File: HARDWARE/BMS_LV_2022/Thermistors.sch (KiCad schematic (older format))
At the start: 18 parts

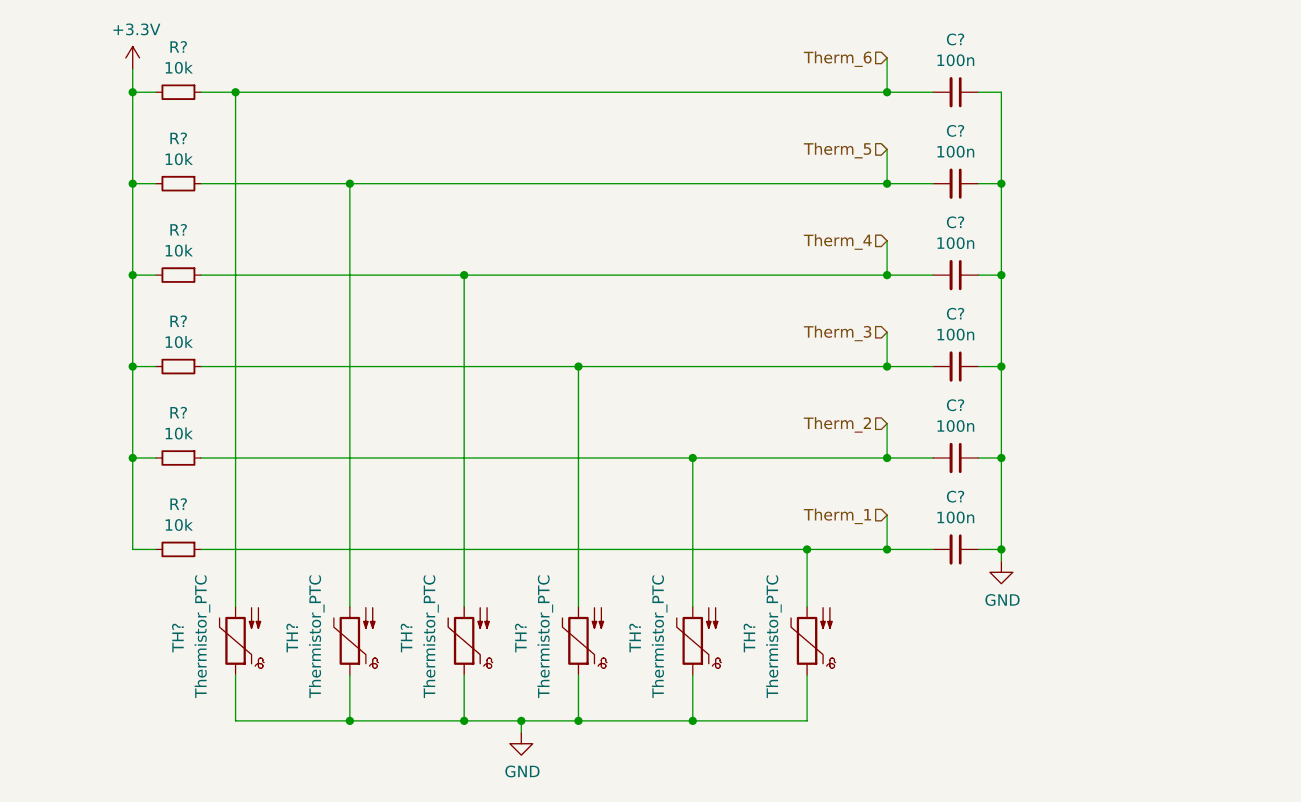
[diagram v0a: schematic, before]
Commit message: Hardware Update 2
First verison of the scheme finished
+Power section
+eFuse section
+Current Sensor section
+Connectors section
+Debug LEDs
+STM32L4P5RET6 all signals configuration
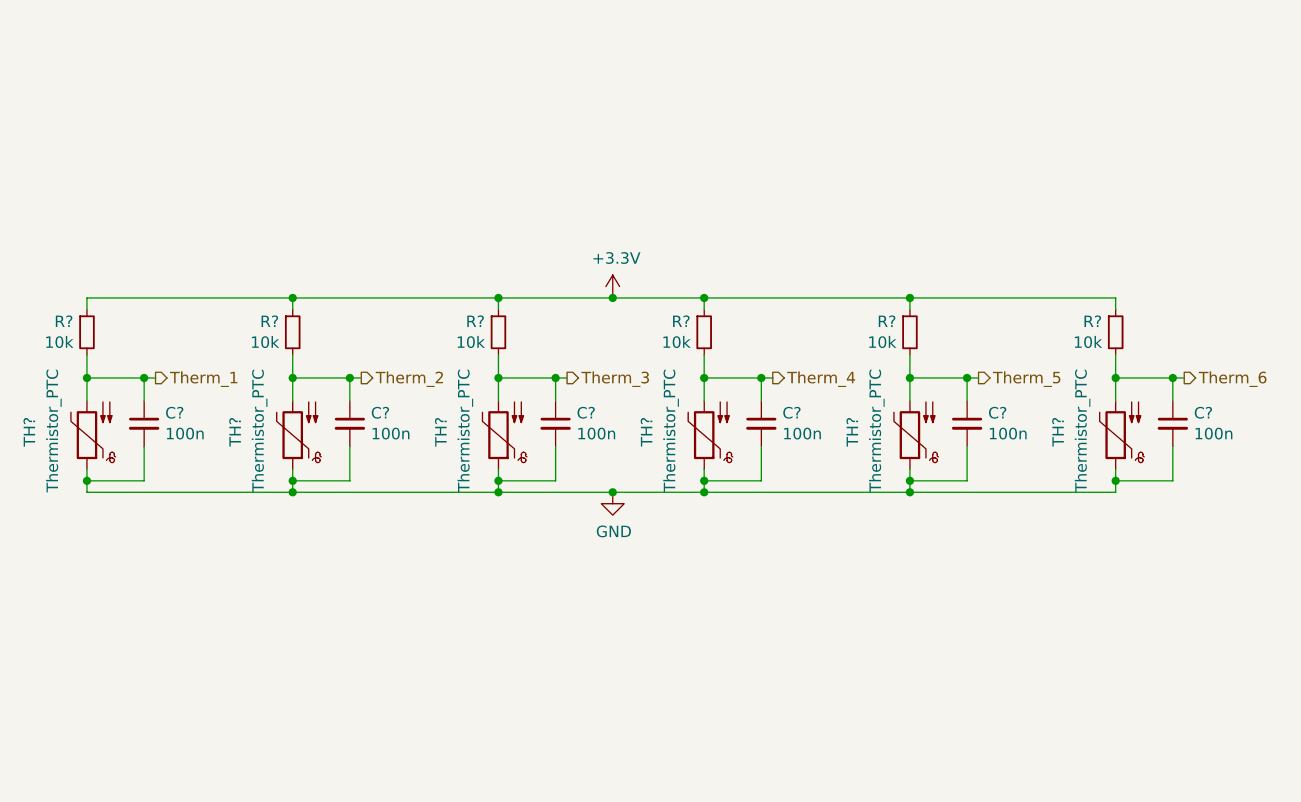
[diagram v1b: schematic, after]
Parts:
- removed C? (x6): 100n, symbol Device:C_Small
- removed R? (x6): 10k, symbol Device:R_Small
- removed TH? (x5): Thermistor_PTC, symbol Device:Thermistor_PTC
- added C? (x6): 100n, symbol Device:C_Small
- added R? (x6): 10k, symbol Device:R_Small
- added TH? (x5): Thermistor_PTC, symbol Device:Thermistor_PTC
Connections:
- net +3V3: now also R?.1, R?.1, R?.1, R?.1, R?.1, R?.1
- net GND: now also C?.2, C?.2, C?.2, C?.2, C?.2, C?.2, TH?.1, TH?.1, TH?.1, TH?.1, TH?.1
- net Therm_1: now also TH?.2, C?.1, R?.2
- net Therm_2: now also C?.1, R?.2, TH?.2
- net Therm_3: now also C?.1, R?.2, TH?.2
- net Therm_4: now also C?.1, R?.2, TH?.2
- net Therm_5: now also C?.1, R?.2, TH?.2
- net Therm_6: now also C?.1, R?.2, TH?.2; no longer TH?.2
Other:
- moved on the sheet: TH?

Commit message: Hardware update; -changes after team review;
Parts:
- C? (x6): value 100n -> 100nF
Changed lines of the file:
@@
 P 1300 2550
 F 0 "C?" H 1392 2596 50  0000 L CNN
-F 1 "100n" H 1392 2505 50  0000 L CNN
+F 1 "100nF" H 1392 2505 50  0000 L CNN
 F 2 "" H 1300 2550 50  0001 C CNN
 F 3 "~" H 1300 2550 50  0001 C CNN
@@
 P 2200 2550
 F 0 "C?" H 2292 2596 50  0000 L CNN
-F 1 "100n" H 2292 2505 50  0000 L CNN
+F 1 "100nF" H 2292 2505 50  0000 L CNN
 F 2 "" H 2200 2550 50  0001 C CNN
 F 3 "~" H 2200 2550 50  0001 C CNN
@@
 P 3100 2550
 F 0 "C?" H 3192 2596 50  0000 L CNN
-F 1 "100n" H 3192 2505 50  0000 L CNN
+F 1 "100nF" H 3192 2505 50  0000 L CNN
 F 2 "" H 3100 2550 50  0001 C CNN
 F 3 "~" H 3100 2550 50  0001 C CNN
@@
 P 4000 2550
 F 0 "C?" H 4092 2596 50  0000 L CNN
-F 1 "100n" H 4092 2505 50  0000 L CNN
+F 1 "100nF" H 4092 2505 50  0000 L CNN
 F 2 "" H 4000 2550 50  0001 C CNN
 F 3 "~" H 4000 2550 50  0001 C CNN
@@
 P 4900 2550
 F 0 "C?" H 4992 2596 50  0000 L CNN
-F 1 "100n" H 4992 2505 50  0000 L CNN
+F 1 "100nF" H 4992 2505 50  0000 L CNN
 F 2 "" H 4900 2550 50  0001 C CNN
 F 3 "~" H 4900 2550 50  0001 C CNN
@@
 P 5800 2550
 F 0 "C?" H 5892 2596 50  0000 L CNN
-F 1 "100n" H 5892 2505 50  0000 L CNN
+F 1 "100nF" H 5892 2505 50  0000 L CNN
 F 2 "" H 5800 2550 50  0001 C CNN
 F 3 "~" H 5800 2550 50  0001 C CNN

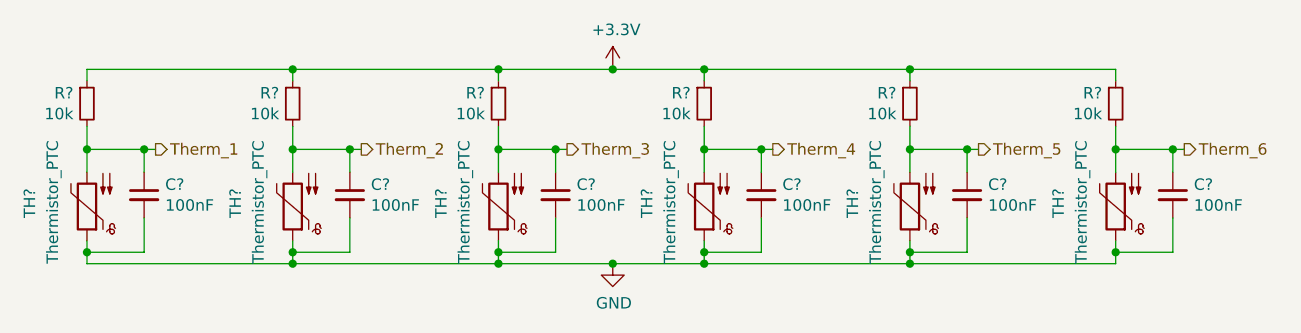
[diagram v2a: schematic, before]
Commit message: Electrical Rules Checker fixes
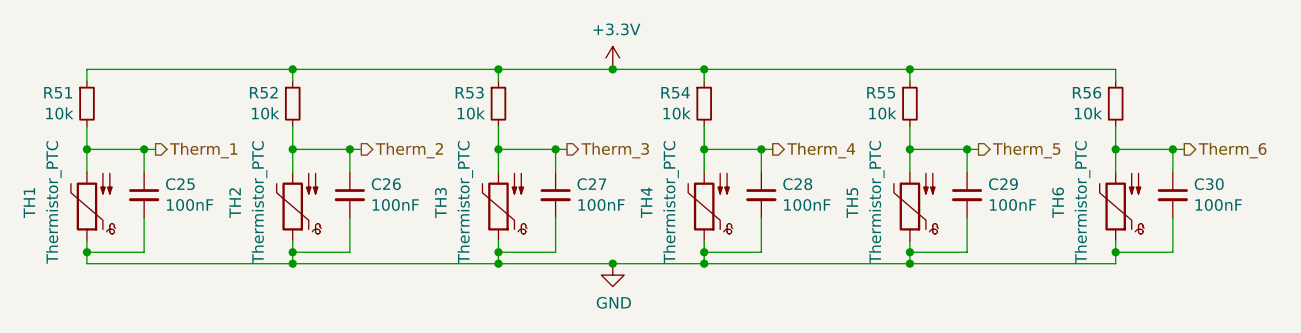
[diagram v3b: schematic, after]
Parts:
- gave numbers to parts that had none: 18
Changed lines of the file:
@@
 Therm_3
 $Comp
-L Device:Thermistor_PTC TH?
+L Device:Thermistor_PTC TH2
 U 1 1 61B219CC
 P 1950 2600
-F 0 "TH?" V 2200 2650 50  0000 R CNN
+F 0 "TH2" V 2200 2650 50  0000 R CNN
 F 1 "Thermistor_PTC" V 2100 2850 50  0000 R CNN
 F 2 "" H 2000 2400 50  0001 L CNN
@@
 	2200 2450 2200 2350
 $Comp
-L Device:Thermistor_PTC TH?
+L Device:Thermistor_PTC TH3
 U 1 1 61B244E9
 P 2850 2600
-F 0 "TH?" V 3100 2650 50  0000 R CNN
+F 0 "TH3" V 3100 2650 50  0000 R CNN
 F 1 "Thermistor_PTC" V 3000 2850 50  0000 R CNN
 F 2 "" H 2900 2400 50  0001 L CNN
@@
 $EndComp
 $Comp
-L power:GND #PWR?
+L power:GND #PWR039
 U 1 1 61B244EF
 P 3350 2850
-F 0 "#PWR?" H 3350 2600 50  0001 C CNN
+F 0 "#PWR039" H 3350 2600 50  0001 C CNN
 F 1 "GND" H 3355 2677 50  0000 C CNN
 F 2 "" H 3350 2850 50  0001 C CNN
@@
 $EndComp
 $Comp
-L power:+3.3V #PWR?
+L power:+3.3V #PWR038
 U 1 1 61B244FC
 P 3350 2000
-F 0 "#PWR?" H 3350 1850 50  0001 C CNN
+F 0 "#PWR038" H 3350 1850 50  0001 C CNN
 F 1 "+3.3V" H 3365 2173 50  0000 C CNN
 F 2 "" H 3350 2000 50  0001 C CNN
@@
 	5550 2000 5550 2050
 $Comp
-L Device:Thermistor_PTC TH?
+L Device:Thermistor_PTC TH6
 U 1 1 61B31D1D
 P 5550 2600
-F 0 "TH?" V 5800 2650 50  0000 R CNN
+F 0 "TH6" V 5800 2650 50  0000 R CNN
 F 1 "Thermistor_PTC" V 5700 2850 50  0000 R CNN
 F 2 "" H 5600 2400 50  0001 L CNN
@@
 	4650 2000 4650 2050
 $Comp
-L Device:Thermistor_PTC TH?
+L Device:Thermistor_PTC TH5
 U 1 1 61B2C7C1
 P 4650 2600
-F 0 "TH?" V 4900 2650 50  0000 R CNN
+F 0 "TH5" V 4900 2650 50  0000 R CNN
 F 1 "Thermistor_PTC" V 4800 2850 50  0000 R CNN
 F 2 "" H 4700 2400 50  0001 L CNN
@@
 	3750 2000 3750 2050
 $Comp
-L Device:Thermistor_PTC TH?
+L Device:Thermistor_PTC TH4
 U 1 1 61B27A00
 P 3750 2600
-F 0 "TH?" V 4000 2650 50  0000 R CNN
+F 0 "TH4" V 4000 2650 50  0000 R CNN
 F 1 "Thermistor_PTC" V 3900 2850 50  0000 R CNN
 F 2 "" H 3800 2400 50  0001 L CNN
@@
 Connection ~ 3350 2850
 $Comp
-L Device:R_Small R?
+L Device:R_Small R52
 U 1 1 62CFDB9E
 P 1950 2150
-F 0 "R?" H 1891 2196 50  0000 R CNN
+F 0 "R52" H 1891 2196 50  0000 R CNN
 F 1 "10k" H 1891 2105 50  0000 R CNN
 F 2 "" H 1950 2150 50  0001 C CNN
@@
 $EndComp
 $Comp
-L Device:R_Small R?
+L Device:R_Small R53
 U 1 1 62CFF2A0
 P 2850 2150
-F 0 "R?" H 2791 2196 50  0000 R CNN
+F 0 "R53" H 2791 2196 50  0000 R CNN
 F 1 "10k" H 2791 2105 50  0000 R CNN
 F 2 "" H 2850 2150 50  0001 C CNN
@@
 $EndComp
 $Comp
-L Device:R_Small R?
+L Device:R_Small R54
 U 1 1 62D007FE
 P 3750 2150
-F 0 "R?" H 3691 2196 50  0000 R CNN
+F 0 "R54" H 3691 2196 50  0000 R CNN
 F 1 "10k" H 3691 2105 50  0000 R CNN
 F 2 "" H 3750 2150 50  0001 C CNN
@@
 $EndComp
 $Comp
-L Device:R_Small R?
+L Device:R_Small R55
 U 1 1 62D01C61
 P 4650 2150
-F 0 "R?" H 4591 2196 50  0000 R CNN
+F 0 "R55" H 4591 2196 50  0000 R CNN
 F 1 "10k" H 4591 2105 50  0000 R CNN
 F 2 "" H 4650 2150 50  0001 C CNN
@@
 $EndComp
 $Comp
-L Device:R_Small R?
+L Device:R_Small R56
 U 1 1 62D030DD
 P 5550 2150
-F 0 "R?" H 5491 2196 50  0000 R CNN
+F 0 "R56" H 5491 2196 50  0000 R CNN
 F 1 "10k" H 5491 2105 50  0000 R CNN
 F 2 "" H 5550 2150 50  0001 C CNN
@@
 	1350 2350 1300 2350
 $Comp
-L Device:R_Small R?
+L Device:R_Small R51
 U 1 1 62CF3EC5
 P 1050 2150
-F 0 "R?" H 991 2196 50  0000 R CNN
+F 0 "R51" H 991 2196 50  0000 R CNN
 F 1 "10k" H 991 2105 50  0000 R CNN
 F 2 "" H 1050 2150 50  0001 C CNN
@@
 Therm_1
 $Comp
-L Device:Thermistor_PTC TH?
+L Device:Thermistor_PTC TH1
 U 1 1 61D11206
 P 1050 2600
-F 0 "TH?" V 1300 2650 50  0000 R CNN
+F 0 "TH1" V 1300 2650 50  0000 R CNN
 F 1 "Thermistor_PTC" V 1200 2850 50  0000 R CNN
 F 2 "" H 1100 2400 50  0001 L CNN
@@
 	4650 2000 5550 2000
 $Comp
-L Device:C_Small C?
+L Device:C_Small C25
 U 1 1 62D3AF1E
 P 1300 2550
-F 0 "C?" H 1392 2596 50  0000 L CNN
+F 0 "C25" H 1392 2596 50  0000 L CNN
 F 1 "100nF" H 1392 2505 50  0000 L CNN
 F 2 "" H 1300 2550 50  0001 C CNN
@@
 $EndComp
 $Comp
-L Device:C_Small C?
+L Device:C_Small C26
 U 1 1 62D3D09F
 P 2200 2550
-F 0 "C?" H 2292 2596 50  0000 L CNN
+F 0 "C26" H 2292 2596 50  0000 L CNN
 F 1 "100nF" H 2292 2505 50  0000 L CNN
 F 2 "" H 2200 2550 50  0001 C CNN
@@
 $EndComp
 $Comp
-L Device:C_Small C?
+L Device:C_Small C27
 U 1 1 62D3FB8F
 P 3100 2550
-F 0 "C?" H 3192 2596 50  0000 L CNN
+F 0 "C27" H 3192 2596 50  0000 L CNN
 F 1 "100nF" H 3192 2505 50  0000 L CNN
 F 2 "" H 3100 2550 50  0001 C CNN
@@
 $EndComp
 $Comp
-L Device:C_Small C?
+L Device:C_Small C28
 U 1 1 62D42810
 P 4000 2550
-F 0 "C?" H 4092 2596 50  0000 L CNN
+F 0 "C28" H 4092 2596 50  0000 L CNN
 F 1 "100nF" H 4092 2505 50  0000 L CNN
 F 2 "" H 4000 2550 50  0001 C CNN
@@
 $EndComp
 $Comp
-L Device:C_Small C?
+L Device:C_Small C29
 U 1 1 62D45530
 P 4900 2550
-F 0 "C?" H 4992 2596 50  0000 L CNN
+F 0 "C29" H 4992 2596 50  0000 L CNN
 F 1 "100nF" H 4992 2505 50  0000 L CNN
 F 2 "" H 4900 2550 50  0001 C CNN
@@
 $EndComp
 $Comp
-L Device:C_Small C?
+L Device:C_Small C30
 U 1 1 62D482C3
 P 5800 2550
-F 0 "C?" H 5892 2596 50  0000 L CNN
+F 0 "C30" H 5892 2596 50  0000 L CNN
 F 1 "100nF" H 5892 2505 50  0000 L CNN
 F 2 "" H 5800 2550 50  0001 C CNN

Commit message: Most of the footprints added
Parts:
- C25, C26, C27, C28, C29, C30: footprint (none) -> Capacitor_SMD:C_0603_1608Metric
- R51, R52, R53, R54, R55, R56: footprint (none) -> Resistor_SMD:R_0603_1608Metric
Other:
- moved on the sheet: C25, C26, C27, C28, C29, C30, R51, R52, R53, R54, R55, R56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

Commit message: PCB layout init
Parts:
- TH1, TH2, TH3, TH4, TH5, TH6: footprint (none) -> Connector_PinHeader_2.54mm:PinHeader_1x02_P2.54mm_Vertical
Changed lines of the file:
@@
 F 0 "TH2" V 4800 4300 50  0000 R CNN
 F 1 "Thermistor_PTC" V 4700 4500 50  0000 R CNN
-F 2 "" H 4600 4050 50  0001 L CNN
+F 2 "Connector_PinHeader_2.54mm:PinHeader_1x02_P2.54mm_Vertical" H 4600 4050 50  0001 L CNN
 F 3 "~" H 4550 4250 50  0001 C CNN
 	1    4550 4250
@@
 F 0 "TH3" V 5700 4300 50  0000 R CNN
 F 1 "Thermistor_PTC" V 5600 4500 50  0000 R CNN
-F 2 "" H 5500 4050 50  0001 L CNN
+F 2 "Connector_PinHeader_2.54mm:PinHeader_1x02_P2.54mm_Vertical" H 5500 4050 50  0001 L CNN
 F 3 "~" H 5450 4250 50  0001 C CNN
 	1    5450 4250
@@
 F 0 "TH6" V 8400 4300 50  0000 R CNN
 F 1 "Thermistor_PTC" V 8300 4500 50  0000 R CNN
-F 2 "" H 8200 4050 50  0001 L CNN
+F 2 "Connector_PinHeader_2.54mm:PinHeader_1x02_P2.54mm_Vertical" H 8200 4050 50  0001 L CNN
 F 3 "~" H 8150 4250 50  0001 C CNN
 	1    8150 4250
@@
 F 0 "TH5" V 7500 4300 50  0000 R CNN
 F 1 "Thermistor_PTC" V 7400 4500 50  0000 R CNN
-F 2 "" H 7300 4050 50  0001 L CNN
+F 2 "Connector_PinHeader_2.54mm:PinHeader_1x02_P2.54mm_Vertical" H 7300 4050 50  0001 L CNN
 F 3 "~" H 7250 4250 50  0001 C CNN
 	1    7250 4250
@@
 F 0 "TH4" V 6600 4300 50  0000 R CNN
 F 1 "Thermistor_PTC" V 6500 4500 50  0000 R CNN
-F 2 "" H 6400 4050 50  0001 L CNN
+F 2 "Connector_PinHeader_2.54mm:PinHeader_1x02_P2.54mm_Vertical" H 6400 4050 50  0001 L CNN
 F 3 "~" H 6350 4250 50  0001 C CNN
 	1    6350 4250
@@
 F 0 "TH1" V 3900 4300 50  0000 R CNN
 F 1 "Thermistor_PTC" V 3800 4500 50  0000 R CNN
-F 2 "" H 3700 4050 50  0001 L CNN
+F 2 "Connector_PinHeader_2.54mm:PinHeader_1x02_P2.54mm_Vertical" H 3700 4050 50  0001 L CNN
 F 3 "~" H 3650 4250 50  0001 C CNN
 	1    3650 4250

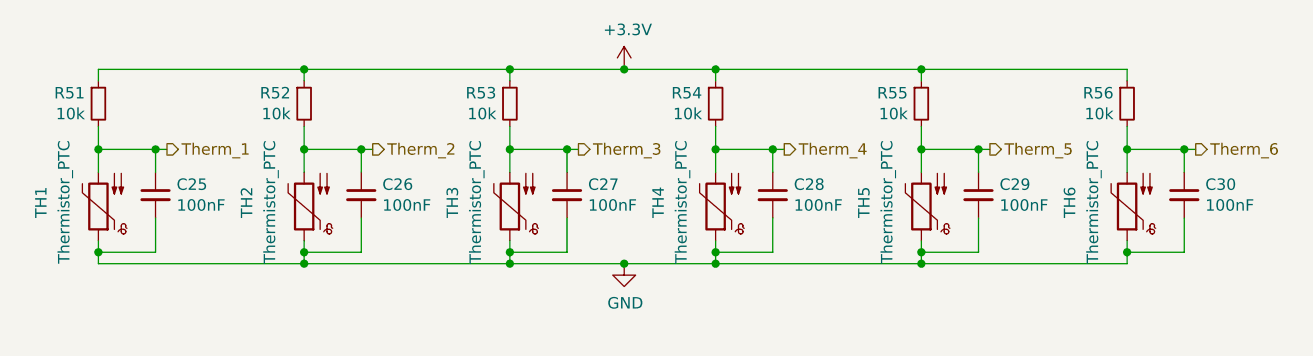
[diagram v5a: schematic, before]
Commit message: Thermistors change
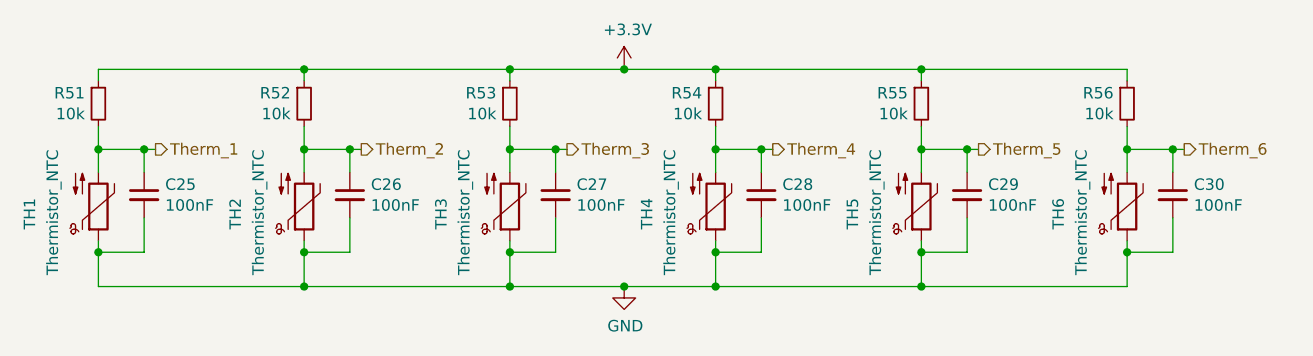
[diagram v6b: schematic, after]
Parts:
- removed TH1, TH2, TH3, TH4, TH5, TH6: Thermistor_PTC, Connector_PinHeader_2.54mm:PinHeader_1x02_P2.54mm_Vertical, symbol Device:Thermistor_PTC
- added TH1, TH2, TH3, TH4, TH5, TH6: Thermistor_NTC, Connector_PinHeader_2.54mm:PinHeader_1x02_P2.54mm_Vertical, symbol Device:Thermistor_NTC
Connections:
- net GND: now also TH1.1, TH2.1, TH3.1, TH4.1, TH5.1, TH6.1
- net Therm_1: now also TH1.2
- net Therm_2: now also TH2.2
- net Therm_3: now also TH3.2
- net Therm_4: now also TH4.2
- net Therm_5: now also TH5.2
- net Therm_6: now also TH6.2
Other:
- moved on the sheet: C25, C26, C27, C28, C29, C30

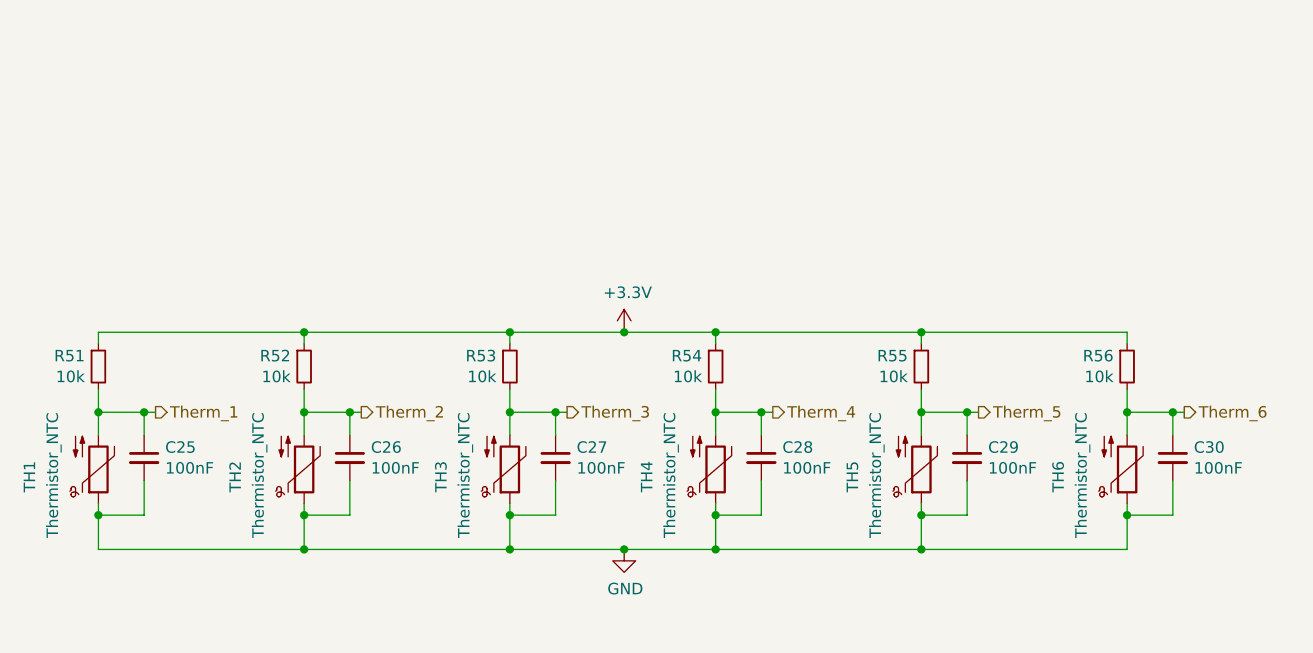
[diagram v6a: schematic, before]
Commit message: PCB update
Parts changed due to smaller footprints
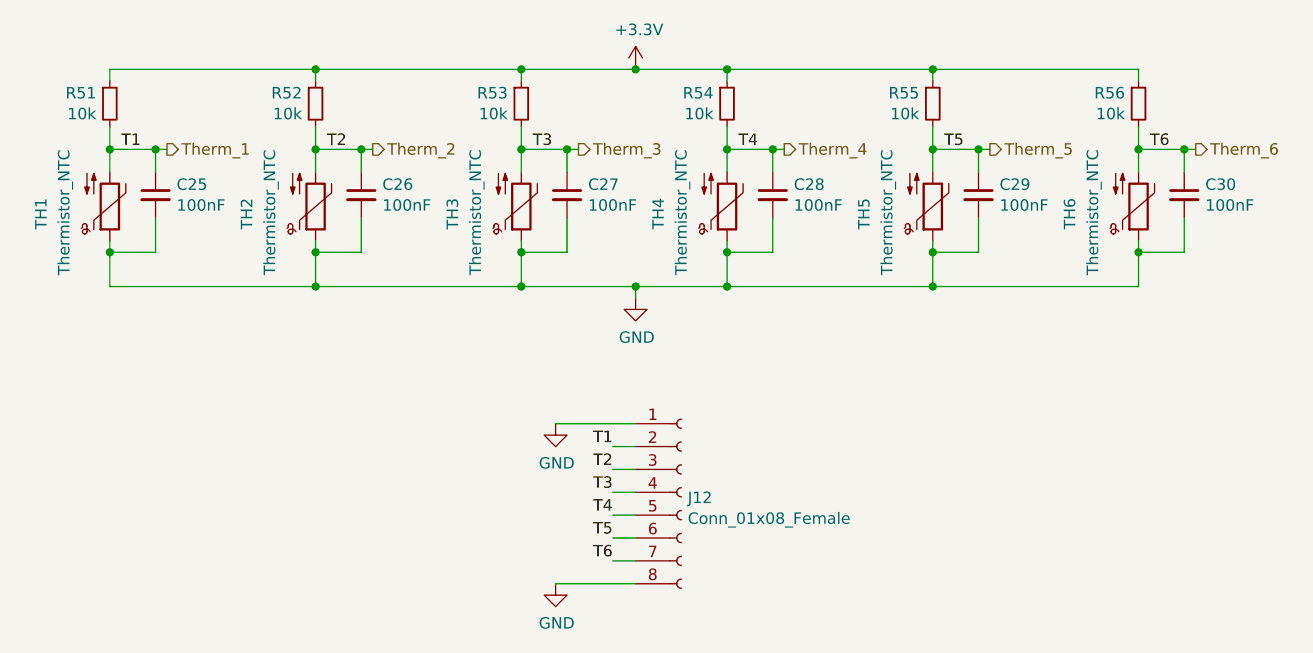
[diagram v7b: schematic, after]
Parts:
- added J12: Conn_01x08_Female, Connector_JST:JST_XH_B8B-XH-A_1x08_P2.50mm_Vertical, symbol Connector:Conn_01x08_Female
- TH1, TH2, TH3, TH4, TH5, TH6: footprint Connector_PinHeader_2.54mm:PinHeader_1x02_P2.54mm_Vertical -> (none)
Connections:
- net GND: now also J12.1 (Pin_1), J12.8 (Pin_8)
- net Therm_1: now also J12.2 (Pin_2)
- net Therm_2: now also J12.3 (Pin_3)
- net Therm_3: now also J12.4 (Pin_4)
- net Therm_4: now also J12.5 (Pin_5)
- net Therm_5: now also J12.6 (Pin_6)
- net Therm_6: now also J12.7 (Pin_7)
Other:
- moved on the sheet: C25, C26, C27, C28, C29, C30, R51, R52, R53, R54, R55, R56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
